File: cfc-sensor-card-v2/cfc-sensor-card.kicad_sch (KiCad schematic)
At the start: 5 parts, among them J1 Conn_01x02

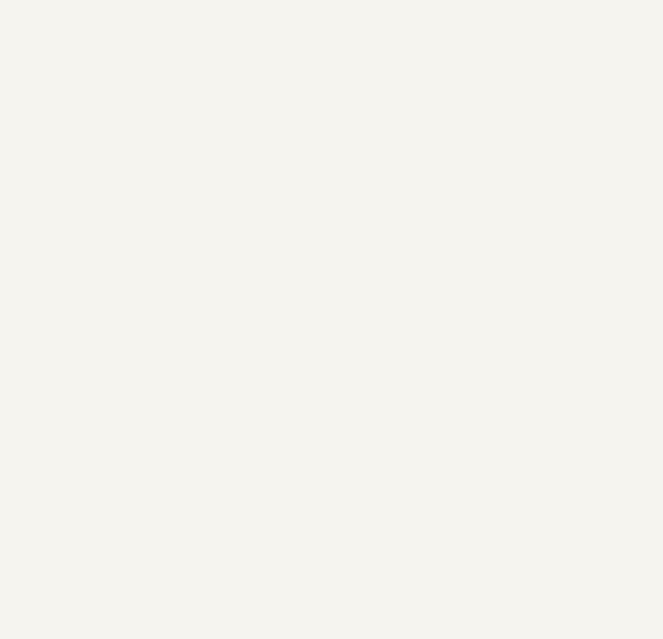
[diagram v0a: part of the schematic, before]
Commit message: Adding PIRT sensor. Needs a double check, and the rest of the symbol.
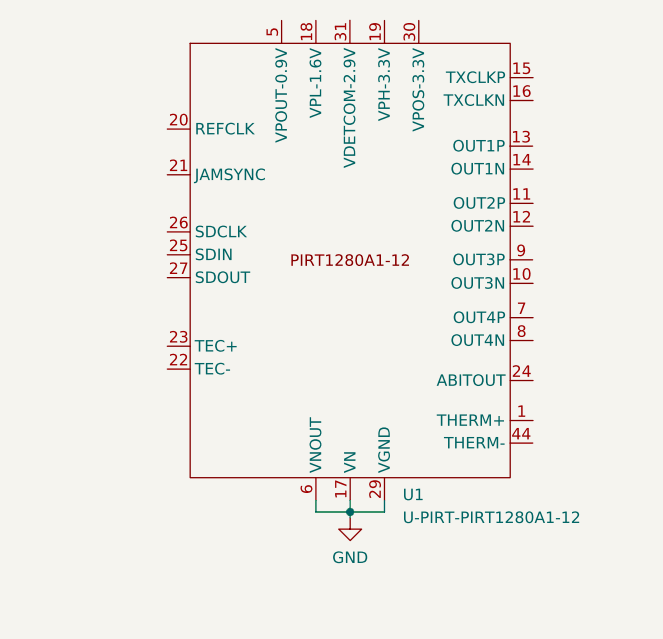
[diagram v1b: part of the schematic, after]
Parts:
- added U1: U-PIRT-PIRT1280A1-12, U-PIR-PIRT1280A1-12:PIRT1280A1-12, symbol U-PIRT-PIRT1280:U-PIRT-PIRT1280A1-12
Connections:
- net GND: now also U1.17 (VN), U1.29 (VGND), U1.6 (VNOUT)
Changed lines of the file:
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@@
   (junction (at 90.805 86.995) (diameter 0) (color 0 0 0 0)
   )
+  (junction (at 167.005 109.855) (diameter 0) (color 0 0 0 0)
+  )
+  (wire (pts (xy 167.005 109.855) (xy 167.005 110.49))
+    (stroke (width 0) (type default) (color 0 0 0 0))
+  )
+  (wire (pts (xy 167.005 109.855) (xy 170.815 109.855))
+    (stroke (width 0) (type default) (color 0 0 0 0))
+  )
   (wire (pts (xy 90.805 84.455) (xy 90.805 86.995))
     (stroke (width 0) (type default) (color 0 0 0 0))
   )
+  (wire (pts (xy 170.815 109.855) (xy 170.815 108.585))
+    (stroke (width 0) (type default) (color 0 0 0 0))
+  )
+  (wire (pts (xy 167.005 108.585) (xy 167.005 109.855))
+    (stroke (width 0) (type default) (color 0 0 0 0))
+  )
   (wire (pts (xy 90.805 86.995) (xy 90.805 90.805))
     (stroke (width 0) (type default) (color 0 0 0 0))
   )
+  (wire (pts (xy 163.195 108.585) (xy 163.195 109.855))
+    (stroke (width 0) (type default) (color 0 0 0 0))
+  )
+  (wire (pts (xy 163.195 109.855) (xy 167.005 109.855))
+    (stroke (width 0) (type default) (color 0 0 0 0))
+  )
   (symbol (lib_id "Mechanical:MountingHole") (at 86.36 110.49 0) (unit 1)
     (in_bom yes) (on_board yes) (fields_autoplaced)
@@
       (effects (font (size 1.27 1.27)) hide)
     )
+  )
+  (symbol (lib_id "power:GND") (at 167.005 110.49 0) (unit 1)
+    (in_bom yes) (on_board yes) (fields_autoplaced)
+    (property "Reference" "#PWR02" (id 0) (at 167.005 116.84 0)
+      (effects (font (size 1.27 1.27)) hide)
+    )
+    (property "Value" "GND" (id 1) (at 167.005 114.935 0))
+    (property "Footprint" "" (id 2) (at 167.005 110.49 0)
+      (effects (font (size 1.27 1.27)) hide)
+    )
+    (property "Datasheet" "" (id 3) (at 167.005 110.49 0)
+      (effects (font (size 1.27 1.27)) hide)
+    )
+    (pin "1")
   )
   (symbol (lib_id "Mechanical:MountingHole") (at 86.36 114.935 0) (unit 1)
@@
       (effects (font (size 1.27 1.27)) hide)
     )
+  )
+  (symbol (lib_id "U-PIRT-PIRT1280:U-PIRT-PIRT1280A1-12") (at 167.005 81.915 0) (unit 1)
+    (in_bom yes) (on_board yes) (fields_autoplaced)
+    (property "Reference" "U1" (id 0) (at 172.8344 107.95 0)
+      (effects (font (size 1.27 1.27)) (justify left))
+    )
+    (property "Value" "U-PIRT-PIRT1280A1-12" (id 1) (at 172.8344 110.49 0)
+      (effects (font (size 1.27 1.27)) (justify left))
+    )
+    (property "Footprint" "U-PIR-PIRT1280A1-12:PIRT1280A1-12" (id 2) (at 158.115 77.47 0)
+      (effects (font (size 1.27 1.27)) hide)
+    )
+    (property "Datasheet" "" (id 3) (at 158.115 77.47 0)
+      (effects (font (size 1.27 1.27)) hide)
+    )
+    (pin "1")
+    (pin "10")
+    (pin "11")
+    (pin "12")
+    (pin "13")
+    (pin "14")
+    (pin "15")
+    (pin "16")
+    (pin "17")
+    (pin "18")
+    (pin "19")
+    (pin "20")
+    (pin "21")
+    (pin "22")
+    (pin "23")
+    (pin "24")
+    (pin "25")
+    (pin "26")
+    (pin "27")
+    (pin "29")
+    (pin "30")
+    (pin "31")
+    (pin "44")
+    (pin "5")
+    (pin "6")
+    (pin "7")
+    (pin "8")
+    (pin "9")
   )
   (sheet_instances
@@
       (reference "#PWR01") (unit 1) (value "GND") (footprint "")
     )
+    (path "/7e8fe9d3-5559-4e50-ba1f-83fd9143e2c8"
+      (reference "#PWR02") (unit 1) (value "GND") (footprint "")
+    )
     (path "/3ae4edbd-179f-4864-80c4-49ca6695971b"
       (reference "H1") (unit 1) (value "MountingHole") (footprint "MountingHole:MountingHole_4.5mm")
@@
       (reference "J1") (unit 1) (value "Conn_01x02") (footprint "Connector_PinHeader_2.54mm:PinHeader_1x02_P2.54mm_Vertical")
     )
-  )
+    (path "/da04be39-8a07-4fbb-9c94-ee3d03a63b2c"
+      (reference "U1") (unit 1) (value "U-PIRT-PIRT1280A1-12") (footprint "U-PIR-PIRT1280A1-12:PIRT1280A1-12")
+    )
+  )

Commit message: feat: cfc sensor card v2
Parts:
- removed H1, H2, H3, H4: MountingHole, MountingHole:MountingHole_4.5mm, symbol Mechanical:MountingHole
- removed J1: Conn_01x02, Connector_PinHeader_2.54mm:PinHeader_1x02_P2.54mm_Vertical, symbol Connector_Generic:Conn_01x02
- removed U1: U-PIRT-PIRT1280A1-12, U-PIR-PIRT1280A1-12:PIRT1280A1-12, symbol U-PIRT-PIRT1280:U-PIRT-PIRT1280A1-12
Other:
- added sheet connectors (connectors.kicad_sch)
- added sheet opd (opd.kicad_sch)
- added sheet pirt (pirt.kicad_sch)

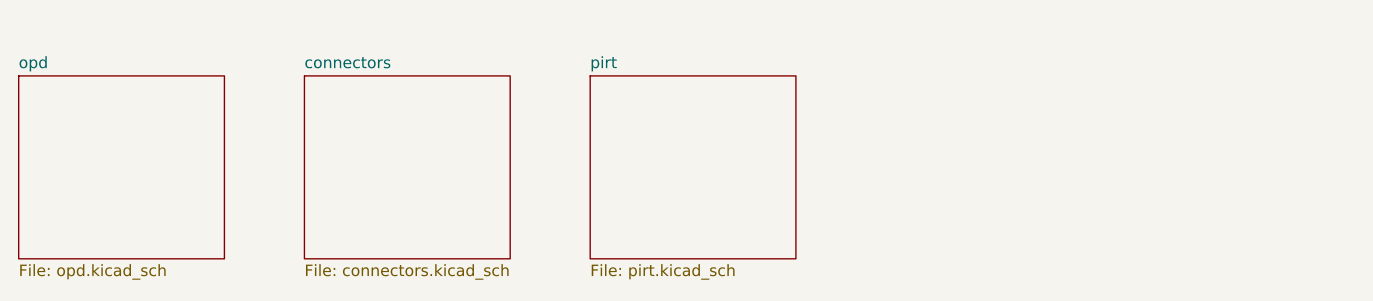
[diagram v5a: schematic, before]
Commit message: Big sweep through to clean up from v2.0 to v2.1 board. Cleaned up all of the Github issues, and even added a MPS2410A CC driver to run the TEC for increased efficiency. Left old switch on board just in case. Lots of cleanup, added some documentation, added pin holes for 1.5 mm alignment pins, now version 2.1
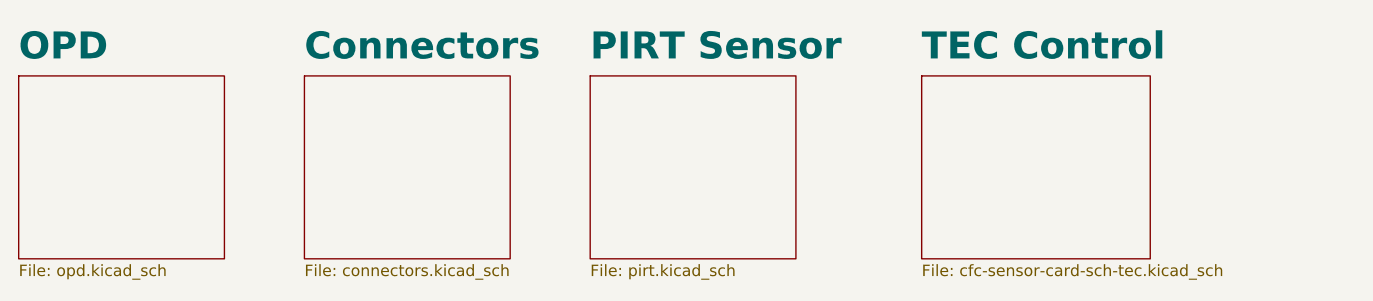
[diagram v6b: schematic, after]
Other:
- sheet connectors renamed Connectors
- sheet opd renamed OPD
- sheet pirt renamed PIRT Sensor
- added sheet TEC Control (cfc-sensor-card-sch-tec.kicad_sch)
- company: (none) -> Portland State Aerospace Society
- title: (none) -> CFC Sensor Card
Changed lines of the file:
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@@
-(kicad_sch (version 20230121) (generator eeschema)
-  (paper "B")
-  (sheet (at 34.29 29.21) (size 22.86 20.32) (fields_autoplaced)
-    (stroke (width 0.1524) (type solid))
-    (fill (color 0 0 0 0.0000))
-    (property "Sheetname" "opd" (at 34.29 28.4984 0)
-      (effects (font (size 1.27 1.27)) (justify left bottom))
-    )
-    (property "Sheetfile" "opd.kicad_sch" (at 34.29 50.1146 0)
-      (effects (font (size 1.27 1.27)) (justify left top))
-    )
-    (instances
-      (project "cfc-sensor-card"
-        (path "/8c53300c-27d6-4efc-b05b-8b907d6da3f5" (page "2"))
-      )
-    )
-  )
-  (sheet (at 97.79 29.21) (size 22.86 20.32) (fields_autoplaced)
-    (stroke (width 0.1524) (type solid))
-    (fill (color 0 0 0 0.0000))
-    (property "Sheetname" "pirt" (at 97.79 28.4984 0)
-      (effects (font (size 1.27 1.27)) (justify left bottom))
-    )
-    (property "Sheetfile" "pirt.kicad_sch" (at 97.79 50.1146 0)
-      (effects (font (size 1.27 1.27)) (justify left top))
-    )
-    (instances
-      (project "cfc-sensor-card"
-        (path "/8c53300c-27d6-4efc-b05b-8b907d6da3f5" (page "4"))
-      )
-    )
-  )
-  (sheet (at 66.04 29.21) (size 22.86 20.32) (fields_autoplaced)
-    (stroke (width 0.1524) (type solid))
-    (fill (color 0 0 0 0.0000))
-    (property "Sheetname" "connectors" (at 66.04 28.4984 0)
-      (effects (font (size 1.27 1.27)) (justify left bottom))
-    )
-    (property "Sheetfile" "connectors.kicad_sch" (at 66.04 50.1146 0)
-      (effects (font (size 1.27 1.27)) (justify left top))
-    )
-    (instances
-      (project "cfc-sensor-card"
-        (path "/8c53300c-27d6-4efc-b05b-8b907d6da3f5" (page "3"))
-      )
-    )
-  )
-  (sheet_instances
-    (path "/" (page "1"))
-  )
+(kicad_sch
+	(version 20250114)
+	(generator "eeschema")
+	(generator_version "9.0")
+	(paper "B")
+	(title_block
+		(title "CFC Sensor Card")
+		(date "2025-09-12")
+		(rev "v2.1")
+		(company "Portland State Aerospace Society")
+	)
+	(sheet
+		(at 34.29 29.21)
+		(size 22.86 20.32)
+		(exclude_from_sim no)
+		(in_bom yes)
+		(on_board yes)
+		(dnp no)
+		(fields_autoplaced yes)
+		(stroke
+			(width 0.1524)
+			(type solid)
+		)
+		(fill
+			(color 0 0 0 0.0000)
+		)
+		(property "Sheetname" "OPD"
+			(at 34.29 27.6334 0)
+			(effects
+				(font
+					(size 3 3)
+					(thickness 0.4)
+					(bold yes)
+				)
+				(justify left bottom)
+			)
+		)
+		(property "Sheetfile" "opd.kicad_sch"
+			(at 34.29 50.1146 0)
+			(effects
+				(font
+					(size 1.27 1.27)
+				)
+				(justify left top)
+			)
+		)
+		(instances
+			(project "cfc-sensor-card"
+				(path "/8c53300c-27d6-4efc-b05b-8b907d6da3f5"
+					(page "2")
+				)
+			)
+		)
+	)
+	(sheet
+		(at 97.79 29.21)
+		(size 22.86 20.32)
+		(exclude_from_sim no)
+		(in_bom yes)
+		(on_board yes)
+		(dnp no)
+		(fields_autoplaced yes)
+		(stroke
+			(width 0.1524)
+			(type solid)
+		)
+		(fill
+			(color 0 0 0 0.0000)
+		)
+		(property "Sheetname" "PIRT Sensor"
+			(at 97.79 27.6334 0)
+			(effects
+				(font
+					(size 3 3)
+					(thickness 0.6)
+					(bold yes)
+				)
+				(justify left bottom)
+			)
+		)
+		(property "Sheetfile" "pirt.kicad_sch"
+			(at 97.79 50.1146 0)
+			(effects
+				(font
+					(size 1.27 1.27)
+				)
+				(justify left top)
+			)
+		)
+		(instances
+			(project "cfc-sensor-card"
+				(path "/8c53300c-27d6-4efc-b05b-8b907d6da3f5"
+					(page "4")
+				)
+			)
+		)
+	)
+	(sheet
+		(at 66.04 29.21)
+		(size 22.86 20.32)
+		(exclude_from_sim no)
+		(in_bom yes)
+		(on_board yes)
+		(dnp no)
+		(fields_autoplaced yes)
+		(stroke
+			(width 0.1524)
+			(type solid)
+		)
+		(fill
+			(color 0 0 0 0.0000)
+		)
+		(property "Sheetname" "Connectors"
+			(at 66.04 27.6334 0)
+			(effects
+				(font
+					(size 3 3)
+					(thickness 0.4)
+					(bold yes)
+				)
+				(justify left bottom)
+			)
+		)
+		(property "Sheetfile" "connectors.kicad_sch"
+			(at 66.04 50.1146 0)
+			(effects
+				(font
+					(size 1.27 1.27)
+				)
+				(justify left top)
+			)
+		)
+		(instances
+			(project "cfc-sensor-card"
+				(path "/8c53300c-27d6-4efc-b05b-8b907d6da3f5"
+					(page "3")
+				)
+			)
+		)
+	)
+	(sheet
+		(at 134.62 29.21)
+		(size 25.4 20.32)
+		(exclude_from_sim no)
+		(in_bom yes)
+		(on_board yes)
+		(dnp no)
+		(fields_autoplaced yes)
+		(stroke
+			(width 0.1524)
+			(type solid)
+		)
+		(fill
+			(color 0 0 0 0.0000)
+		)
+		(property "Sheetname" "TEC Control"
+			(at 134.62 27.6334 0)
+			(effects
+				(font
+					(size 3 3)
+					(thickness 0.6)
+					(bold yes)
+				)
+				(justify left bottom)
+			)
+		)
+		(property "Sheetfile" "cfc-sensor-card-sch-tec.kicad_sch"
+			(at 134.62 50.1146 0)
+			(effects
+				(font
+					(size 1.27 1.27)
+				)
+				(justify left top)
+			)
+		)
+		(instances
+			(project "cfc-sensor-card"
+				(path "/8c53300c-27d6-4efc-b05b-8b907d6da3f5"
+					(page "5")
+				)
+			)
+		)
+	)
+	(sheet_instances
+		(path "/"
+			(page "1")
+		)
+	)
+	(embedded_fonts no)
 )
